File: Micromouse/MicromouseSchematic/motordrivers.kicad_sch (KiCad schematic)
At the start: 4 parts, among them J1 Conn_01x06_MountingPin, U7 MP6550GG-Z

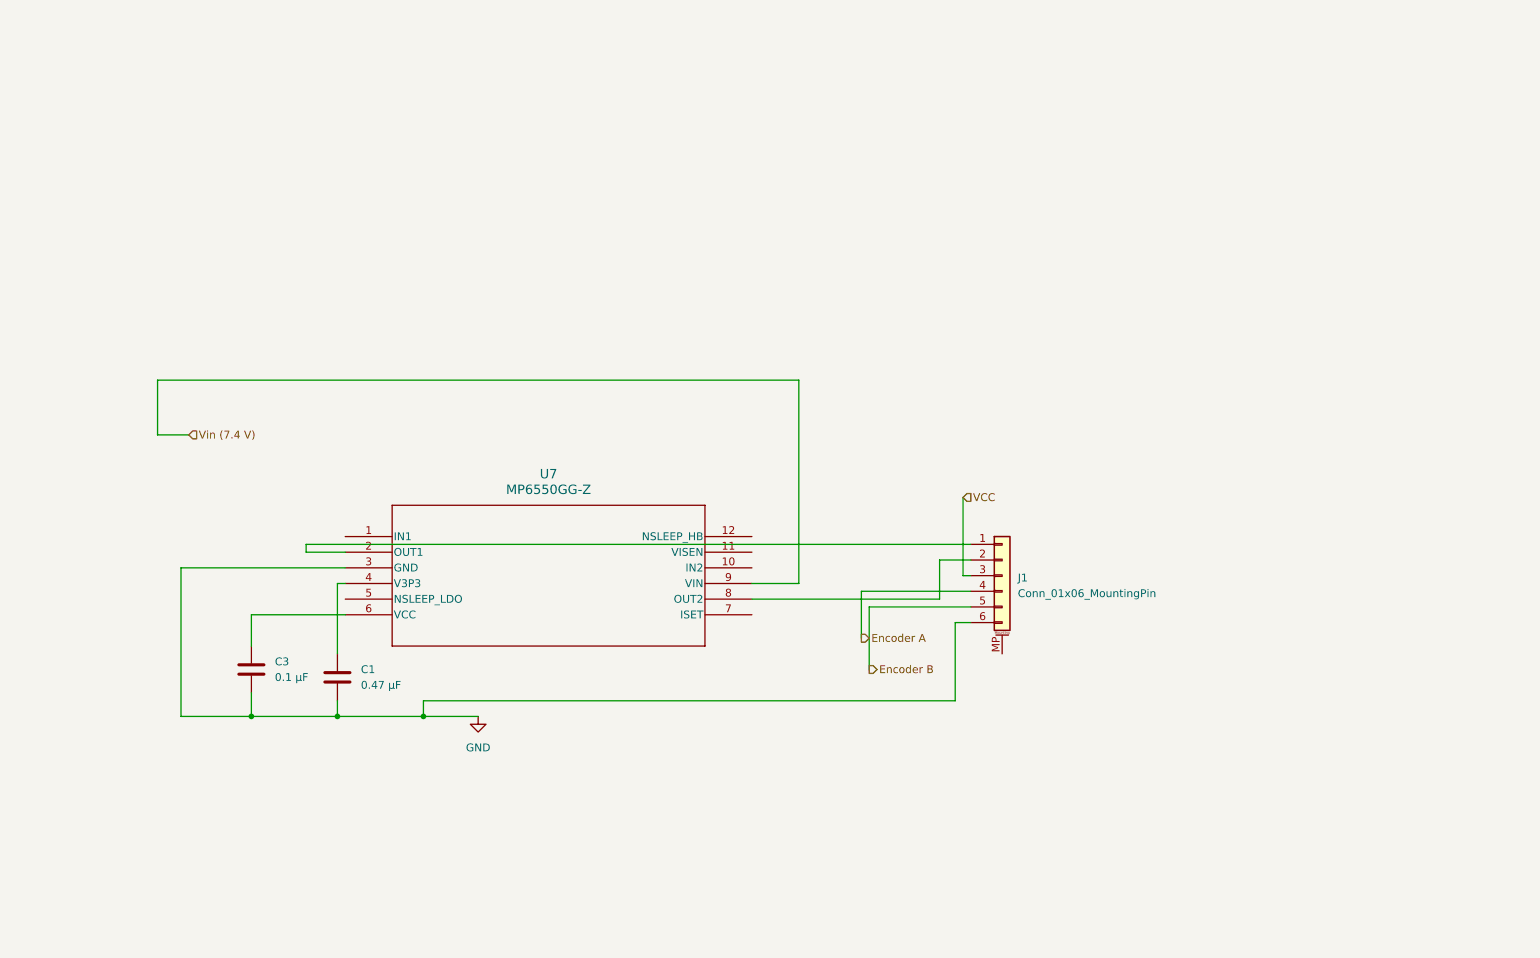
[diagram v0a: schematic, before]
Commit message: changed motor driver schematics
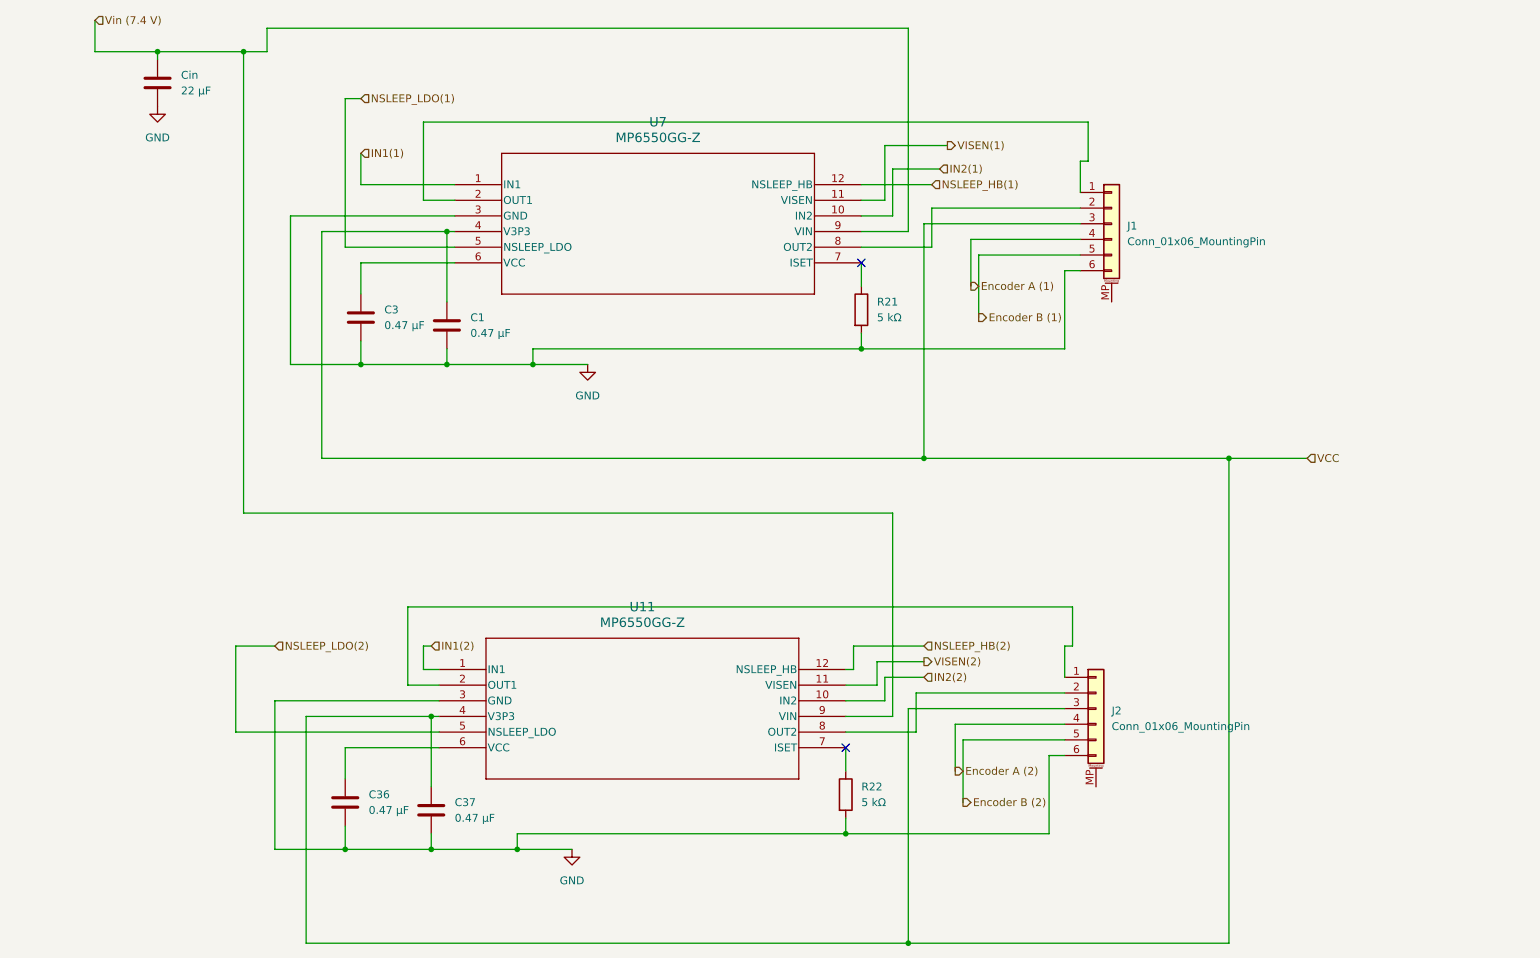
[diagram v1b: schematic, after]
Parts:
- added C36, C37: 0.47 μF, symbol Device:C
- added Cin: 22 μF, symbol Device:C
- added J2: Conn_01x06_MountingPin, symbol Connector_Generic_MountingPin:Conn_01x06_MountingPin
- added R21, R22: 5 kΩ, symbol Device:R
- added U11: MP6550GG-Z, IC12_MP6550_MNP, symbol MP6550GG-Z:MP6550GG-Z
- C3: value 0.1 μF -> 0.47 μF
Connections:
- net GND: now also C36.2, C37.2, Cin.2, J2.6 (Pin_6), R21.2, R22.2, U11.3 (GND)
- net VCC: now also C1.1, U7.4 (V3P3), C37.1, J2.3 (Pin_3), U11.4 (V3P3)
- net Vin (7.4 V): now also Cin.1, U11.9 (VIN)
- net IN1(1): now reaches U7.1 (IN1)
- net IN2(1): now reaches U7.10 (IN2)
- net VISEN(1): now reaches U7.11 (VISEN)
- net NSLEEP_HB(1): now reaches U7.12 (NSLEEP_HB)
- net NSLEEP_LDO(1): now reaches U7.5 (NSLEEP_LDO)
- net at U7.7 (ISET): now also R21.1
- net Encoder A renamed Encoder A (1)
- net Encoder B renamed Encoder B (1)
- new net: J2.1 (Pin_1), U11.2 (OUT1)
- new net: J2.2 (Pin_2), U11.8 (OUT2)
- new net: C36.1, U11.6 (VCC)
- new net: R22.1, U11.7 (ISET)
- new net Encoder A (2): J2.4 (Pin_4)
- new net Encoder B (2): J2.5 (Pin_5)
- new net IN1(2): U11.1 (IN1)
- new net IN2(2): U11.10 (IN2)
- new net NSLEEP_HB(2): U11.12 (NSLEEP_HB)
- new net NSLEEP_LDO(2): U11.5 (NSLEEP_LDO)
- new net VISEN(2): U11.11 (VISEN)
- no-connect marks 0 -> 2
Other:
- moved on the sheet: C1, C3, J1, U7

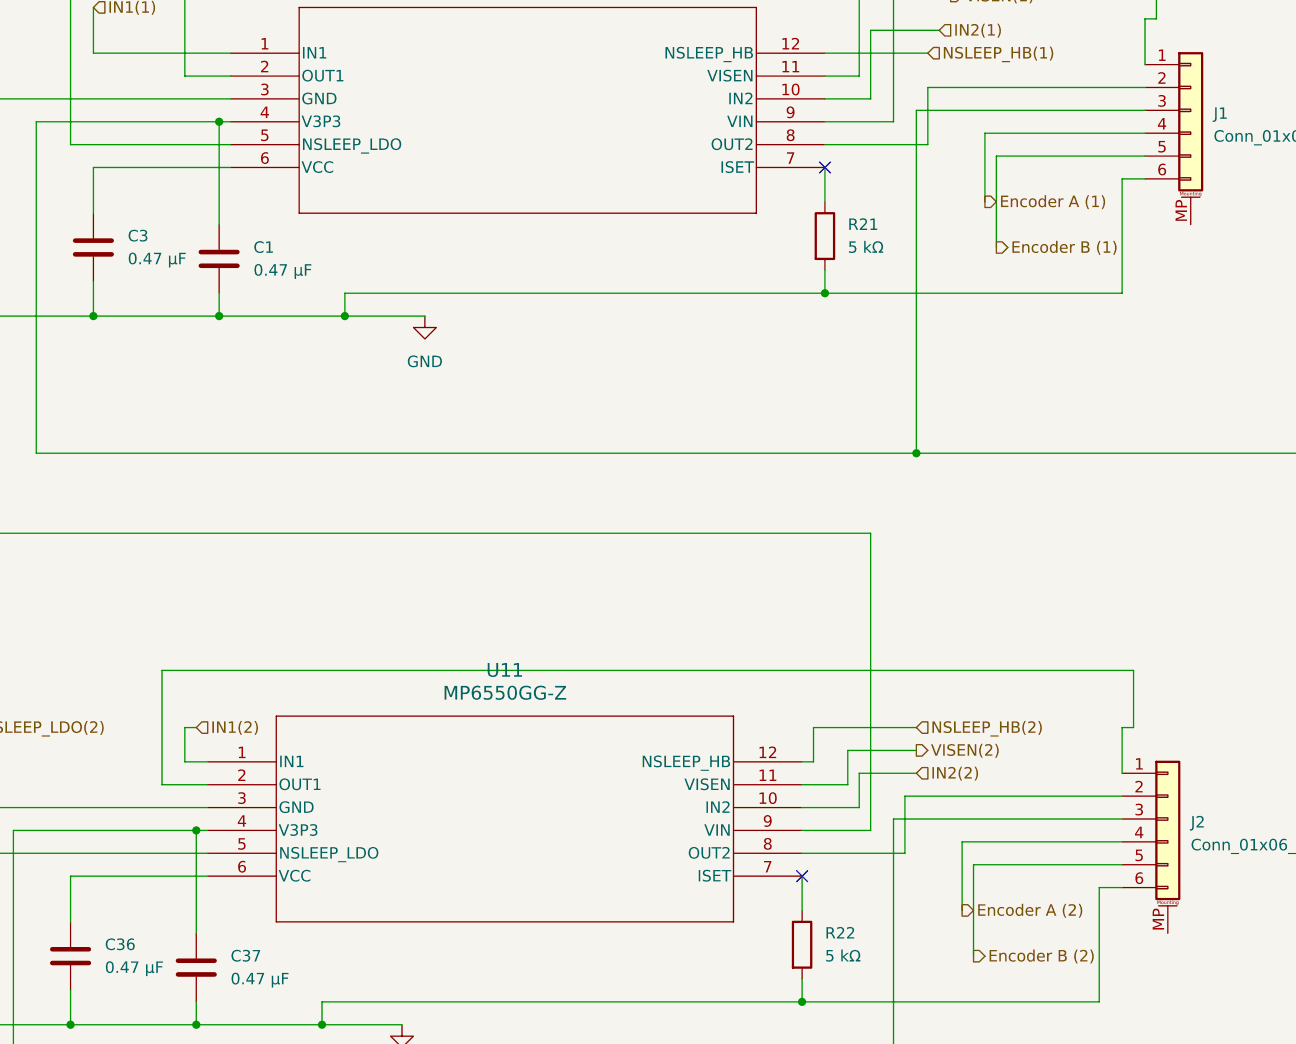
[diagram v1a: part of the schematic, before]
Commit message: Added IR, programming header, i2c & timer pins
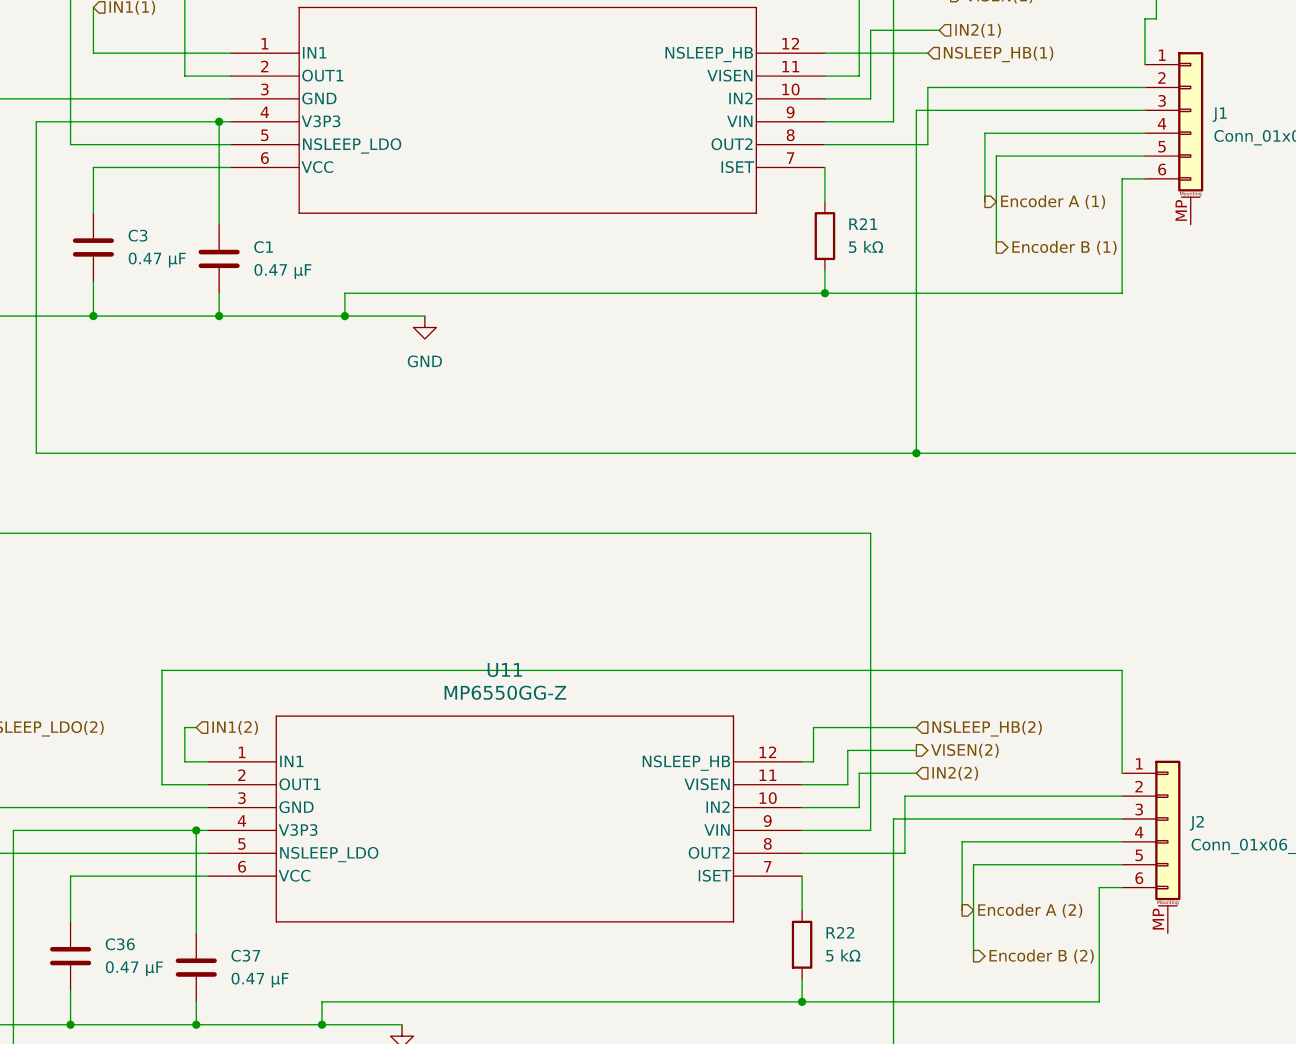
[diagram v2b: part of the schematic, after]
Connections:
- no-connect marks 2 -> 0
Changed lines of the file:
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@@
 		(color 0 0 0 0)
 	)
-	(no_connect
-		(at 148.59 62.23)
-	)
-	(no_connect
-		(at 146.05 140.97)
-	)
 	(wire
 		(pts
@@
 	(wire
 		(pts
-			(xy 182.88 118.11) (xy 182.88 124.46)
+			(xy 181.61 118.11) (xy 181.61 129.54)
 		)
 		(stroke
@@
 	(wire
 		(pts
-			(xy 181.61 124.46) (xy 181.61 129.54)
-		)
-		(stroke
-			(width 0)
-			(type default)
-		)
-	)
-	(wire
-		(pts
 			(xy 55.88 54.61) (xy 55.88 78.74)
 		)
@@
 	(wire
 		(pts
-			(xy 74.93 118.11) (xy 182.88 118.11)
+			(xy 74.93 118.11) (xy 181.61 118.11)
 		)
 		(stroke
@@
 		)
 		(stroke
-			(width 0)
-			(type default)
-		)
-	)
-	(wire
-		(pts
-			(xy 182.88 124.46) (xy 181.61 124.46)
-		)
-		(stroke

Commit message: added some stuff
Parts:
- U11, U7: footprint IC12_MP6550_MNP -> MP655OG-Z_FOOTPRINT:MP6550_MNP
- renumbered Cin to Cin_MD1
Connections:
- no-connect marks 0 -> 2
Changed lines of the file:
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@@
 		(color 0 0 0 0)
+	)
+	(no_connect
+		(at 186.69 147.32)
+	)
+	(no_connect
+		(at 189.23 68.58)
 	)
 	(wire
@@
 			)
 		)
-		(property "Footprint" "IC12_MP6550_MNP"
+		(property "Footprint" "MP655OG-Z_FOOTPRINT:MP6550_MNP"
 			(at 80.01 128.27 0)
 			(effects
@@
 		(dnp no)
 		(fields_autoplaced yes)
-		(property "Reference" "Cin"
+		(property "Reference" "Cin_MD1"
 			(at 38.1 31.7499 0)
 			(effects
@@
 			(project ""
 				(path "/0dcfab91-6b00-43c0-ac0b-8c301cb559e5/cf2a6fe6-71ef-47dc-a740-f3079c853c7d"
-					(reference "Cin")
+					(reference "Cin_MD1")
 					(unit 1)
 				)
@@
 			)
 		)
-		(property "Footprint" "IC12_MP6550_MNP"
+		(property "Footprint" "MP655OG-Z_FOOTPRINT:MP6550_MNP"
 			(at 82.55 49.53 0)
 			(effects

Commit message: Micromouse KiCad: MP6550 libs in project, fp-lib paths, schematic updates
Move MP6550G-Z symbol and legacy footprints into MicromouseSchematic, add
MP6550G-Z.pretty with MP6550_MNP footprint, and point fp-lib-table at the
project-local MM_MP6550G-Z library.

Replace old absolute footprint paths with this repo’s Micromouse tree and
MM_* library names. Update root schematic and IMU/IR/motor/TOF/regulator
subsheets; add empty bluethooth.kicad_sch hierarchical sheet. Extend KiCad
project BOM field configuration; refresh fp-info-cache. Drop schematic lock
file; include dated schematic backup zip.
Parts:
- U11, U7: footprint MP655OG-Z_FOOTPRINT:MP6550_MNP -> MM_MP6550G-Z:MP6550_MNP
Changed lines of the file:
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@@
 			)
 		)
-		(property "Footprint" "MP655OG-Z_FOOTPRINT:MP6550_MNP"
+		(property "Footprint" "MM_MP6550G-Z:MP6550_MNP"
 			(at 80.01 128.27 0)
 			(effects
@@
 			)
 		)
-		(property "Footprint" "MP655OG-Z_FOOTPRINT:MP6550_MNP"
+		(property "Footprint" "MM_MP6550G-Z:MP6550_MNP"
 			(at 82.55 49.53 0)
 			(effects
